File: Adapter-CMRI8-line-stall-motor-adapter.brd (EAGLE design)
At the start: 31 x 50 mm, 16 parts, among them M1 MOUNTINGHOLE, M2 MOUNTINGHOLE

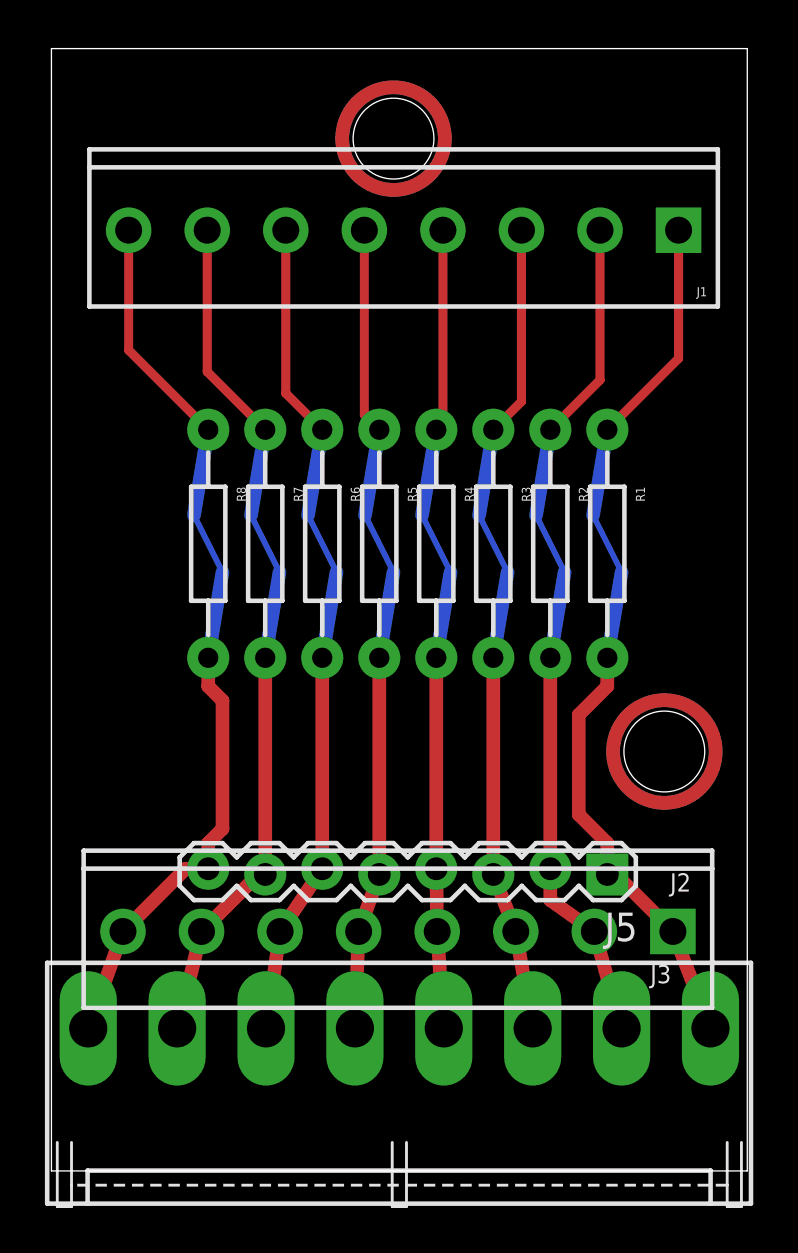
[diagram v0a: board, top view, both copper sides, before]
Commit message: clean up of initial fab order
Misc changes to clean up clearances and documentation for initial build (20211204)
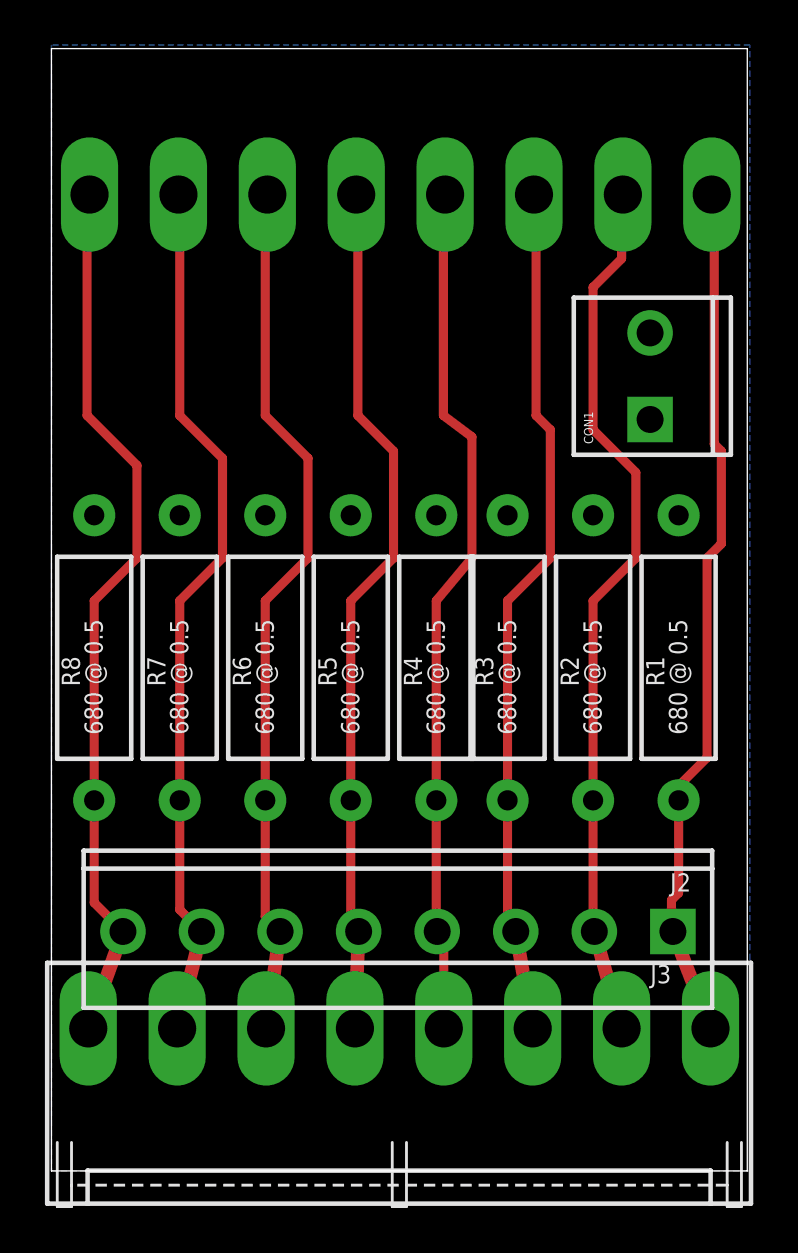
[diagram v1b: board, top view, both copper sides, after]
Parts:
- removed J1: (no value), SPCoast:SCREWTERMINAL-3.5MM-8
- removed J5: (no value), SPCoast:1X08_LOCK
- removed M1, M2: MOUNTINGHOLE, SPCoast:MOUNTINGHOLE
- added CON1: 12V, SPCoast:SCREWTERMINAL-3.5MM-2_LOCK
- added J4: Molex In, SPCoast:KK-156-8-F
- J2: value (none) -> 3.5mm
- J3: value (none) -> Molex Out
- R1, R2, R3, R4, R5, R6, R7, R8: value (none) -> 680 @ 0.5; device SPCoast:AXIAL-0.4-RES -> SparkFun-Resistors:AXIAL-0.5
- U$1: value DOC-OSHW-LOGO-L -> (none); device SPCoast:OSHW-LOGO-L -> MRCS-prop65warningBtm:CA-PROP65WARNING
- moved U$1 24.7 mm to (19.1, 21.6)
- moved U$2 24.2 mm to (0.64, 33.7)
- moved R8 7.18 mm to (1.91, 22.9), turned to 90 degrees
- moved R7 6.35 mm to (5.71, 22.9), turned to 90 degrees
- moved R1 5.99 mm to (27.9, 22.9), turned to 90 degrees
- moved R6 5.68 mm to (9.53, 22.9), turned to 90 degrees
- moved R2 5.43 mm to (24.1, 22.9), turned to 90 degrees
- moved R5 5.24 mm to (13.3, 22.9), turned to 90 degrees
- moved R3 5.12 mm to (20.3, 22.9), turned to 90 degrees
- moved R4 5.08 mm to (17.1, 22.9), turned to 90 degrees
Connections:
- removed net L1: J1.1, J2.1, J3.1, J5.1, R1.P$1, R1.P$2
- removed net L4: J1.4, J2.4, J3.4, J5.4, R4.P$1, R4.P$2
- new net N$1: J2.1, J3.1, J4.1, R1.P$1
- new net N$8: J2.4, J3.4, J4.4, R4.P$1
- new net VIN: CON1.1, CON1.2, R1.P$2, R2.P$2, R3.P$2, R4.P$2, R5.P$2, R6.P$2, R7.P$2, R8.P$2
- net L2: now also J4.2; no longer J1.2, J5.2, R2.P$2
- net L3: now also J4.3; no longer J1.3, J5.3, R3.P$2
- net L5: now also J4.5; no longer J1.5, J5.5, R5.P$2
- net L6: now also J4.6; no longer J1.6, J5.6, R6.P$2
- net L7: now also J4.7; no longer J1.7, J5.7, R7.P$2
- net L8: now also J4.8; no longer J1.8, J5.8, R8.P$2
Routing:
- net L1: track 40.1 -> 0.00 mm
- net N$1: track 0.00 -> 38.6 mm
- net N$8: track 0.00 -> 38.5 mm
- net L4: track 36.1 -> 0.00 mm
- net L5: track 36.8 -> 38.8 mm
- net L6: track 37.3 -> 39.1 mm
- net L2: track 38.1 -> 39.5 mm
- net L3: track 37.5 -> 38.5 mm
- net L7: track 38.5 -> 39.3 mm
- net L8: track 40.4 -> 39.7 mm
- added copper zone on layer 16, net VIN
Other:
- board text added: "CMRI 8 Line Stall Motor Adapter"
- board text added: "CMRI 8 Line Stall MotorAdapter V 1.0 20211204 Seth Neumann"
- board text removed: "8 pin Molex to 3.5mm"
- board text removed: "Breakout"
- board text removed: "CMRI Accessory"
- board text removed: "COMMON"
- board text removed: "CON1"
- board text removed: "Cut on reverse for Resistors"
- board text removed: "J1"
- board text removed: "J2"
- board text removed: "J3"
- board text removed: "J4"
- board text removed: "J5"
- board text removed: "Model Railroading is fun!"
- board text removed: "R1"
- board text removed: "R2"
- board text removed: "R3"
- board text removed: "R4"
- board text removed: "R5"
- board text removed: "R6"
- board text removed: "R7"
- board text removed: "R8"
